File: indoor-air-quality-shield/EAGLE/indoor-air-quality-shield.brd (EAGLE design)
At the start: 160 x 100 mm, 36 parts, among them J4 POWER_JACKSLT, Q1 MMBT2222A, U6 AP1509-50SG-13

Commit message: upadted pcb layout
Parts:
- removed C10: 100uF, 10V, SparkFun-Capacitors:PANASONIC_D
- removed C8: 10nF, SparkFun-Capacitors:0603-CAP
- removed C9: 47uF, 25V, SparkFun-Capacitors:PANASONIC_D
- removed J4: POWER_JACKSLT, Spark:POWER_JACK_SLOT
- removed JP5: M02PTH3, SparkFun-Connectors:1X02_LONGPADS
- removed LED5: BLUE, SparkFun-LED:LED-0603
- removed R13: 1K, SparkFun-Passives:0603-RES
- removed R14, R15: (no value), pot:RJ9W
- removed R16: (no value), SparkFun-Passives:0603-RES
- removed U6: AP1509-50SG-13, Spark:SO08
- added C1: 47uF, 25V, SparkFun-Capacitors:PANASONIC_D
- added C2: 100uF, 10V, SparkFun-Capacitors:PANASONIC_D
- added C3: 10nF, SparkFun-Capacitors:0603-CAP
- added J3: (no value), Connector:4P-2.0
- added JP2: (no value), SparkFun-Connectors:1X03
- added LED1: BLUE, SparkFun-LED:LED-0603
- added R10: 10K, SparkFun-Passives:0603-RES
- added R7, R8, R9: 1K, SparkFun-Passives:0603-RES
- added U1: AP1509-50SG-13, Spark:SO08
- D1: value LED-RGB-CC-THRUCLEAR -> B230; device SparkFun-LED:LED-RGB-THRU -> adafruit:SMADIODE
- D3: value B230 -> LED-RGB-CC-THRUCLEAR; device adafruit:SMADIODE -> SparkFun-LED:LED-RGB-THRU
- J1: value (none) -> POWER_JACKSLT; device Connector:4P-2.0 -> Spark:POWER_JACK_SLOT
- JP1: value (none) -> M02PTH3; device SparkFun-Connectors:1X03 -> SparkFun-Connectors:1X02_LONGPADS
- R1, R2, R3, R4: value (none) -> 50K; device SparkFun-Passives:0603-RES -> pot:RJ9W
- R11, R12: value (none) -> 10K; device pot:RJ9W -> SparkFun-Passives:0603-RES
- R5, R6: value (none) -> 1K
- U$1: value SPARK_CORE -> MQ_SENSOR_SOCKET; device Spark:SPARK_CORE_STACKABLE -> Spark:MQ_SENSOR_SOCKET
- U$3: value MICS5525 -> MQ_SENSOR_SOCKET; device Spark:MICS5525 -> Spark:MQ_SENSOR_SOCKET
- U$4: value MQ_SENSOR_SOCKET -> MICS5525; device Spark:MQ_SENSOR_SOCKET -> Spark:MICS5525
- U$5: value MQ_SENSOR_SOCKET -> DHT22; device Spark:MQ_SENSOR_SOCKET -> Spark:DHT22
- U$6: value DHT22 -> SPARK_CORE; device Spark:DHT22 -> Spark:SPARK_CORE_STACKABLE
- moved JP1 195.4 mm to (99.1, 66.0), turned to 180 degrees
- moved J1 167.7 mm to (102.9, 62.2)
- moved D1 164.8 mm to (106.4, 79.8), turned to 180 degrees
- moved R5 156.6 mm to (125.7, 81.3), turned to 90 degrees
- moved S2 155.4 mm to (82.5, 67.3), turned to 270 degrees
- moved L1 151.3 mm to (119.4, 75.4)
- moved U$6 149.1 mm to (20.3, 81.3), turned to 180 degrees
- moved S1 141.4 mm to (76.2, 67.3), turned to 90 degrees
- moved D2 137.0 mm to (119.1, 82.8)
- moved U$5 135.8 mm to (72.4, 91.4), turned to 270 degrees
- moved R12 135.5 mm to (17.8, 96.5), turned to 180 degrees
- moved U$2 121.1 mm to (63.5, 95.2)
- moved Q1 120.3 mm to (81.3, 73.7), turned to 270 degrees
- moved D3 119.1 mm to (90.2, 66.0), turned to 90 degrees
- moved R6 116.6 mm to (81.3, 77.5)
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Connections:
- net +3V3: now also R10.2, U$5.VDD, U$6.#24, U$6.24, U$6.@24; no longer R16.2, U$1.#24, U$1.24, U$1.@24, U$6.VDD
- net +5V: now also C2.+, C3.2, J3.3, R11.2, R12.2, U$1.5, U$1.6, U$1.7, U$3.5, U$3.6, U$3.7, U$4.H+, U$4.S+, U$6.#1, U$6.1, U$6.@1, U1.3; no longer C10.+, C8.2, J1.3, R13.2, R4.2, U$1.#1, U$1.1, U$1.@1, U$3.H+, U$3.S+, U$4.5, U$4.6, U$4.7, U$5.5, U$5.6, U$5.7, U6.3
- net 3V3*: now also U$6.#22, U$6.22, U$6.@22; no longer U$1.#22, U$1.22, U$1.@22
- net BLUE: now also R7.2, U$6.#5, U$6.5, U$6.@5; no longer R3.2, U$1.#5, U$1.5, U$1.@5
- net BTN1: now also U$6.#16, U$6.16, U$6.@16; no longer U$1.#16, U$1.16, U$1.@16
- net BTN2: now also U$6.#17, U$6.17, U$6.@17; no longer U$1.#17, U$1.17, U$1.@17
- net BUZZER: now also U$6.#8, U$6.8, U$6.@8
- net DHT22: now also R10.1, U$5.DATA, U$6.#15, U$6.15, U$6.@15; no longer R16.1, U$1.#15, U$1.15, U$1.@15, U$6.DATA
- net GND: now also C1.-, C2.-, C3.1, D3.2, J1.GND@1, J1.GND@2, J3.4, JP2.1, LED1.C, R1.A, R1.S, R2.A, R2.S, R3.A, R3.S, R4.A, R4.S, U$4.H-, U$5.GND, U$6.#2, U$6.#21, U$6.2, U$6.21, U$6.@2, U$6.@21, U1.4, U1.5, U1.6, U1.7, U1.8; no longer C10.-, C8.1, C9.-, D1.2, J1.4, J4.GND@1, J4.GND@2, JP5.1, LED5.C, R11.A, R11.S, R12.A, R12.S, R14.A, R14.S, R15.A, R15.S, U$1.#2, U$1.#21, U$1.2, U$1.21, U$1.@2, U$1.@21, U$3.H-, U$6.GND, U6.4, U6.5, U6.6, U6.7, U6.8
- net GREEN: now also R8.2, U$6.#6, U$6.6, U$6.@6; no longer R2.2, U$1.#6, U$1.6, U$1.@6
- net MICS: now also R3.E, U$4.S-, U$6.#11, U$6.11, U$6.@11; no longer R12.E, U$1.#11, U$1.11, U$1.@11, U$3.S-
- net MQ1: now also R2.E, U$1.1, U$1.3, U$6.#10, U$6.10, U$6.@10; no longer R14.E, U$1.#10, U$1.10, U$1.@10, U$4.1, U$4.3
- net MQ2: now also R4.E, U$3.1, U$3.3, U$6.#9, U$6.9, U$6.@9; no longer R15.E, U$1.#9, U$1.9, U$1.@9, U$5.1, U$5.3
- net N$1: now also D3.4, R7.1; no longer D1.4, R3.1
- net N$14: now also C1.+, D1.C, U1.1; no longer C9.+, D3.C, U6.1
- net N$16: now also LED1.A, R5.1; no longer LED5.A, R13.1
- net N$2: now also D3.3, R8.1; no longer D1.3, R2.1
- net N$3: now also D3.1, R9.1; no longer D1.1, R1.1
- net N$32: now also D1.A, J1.PWR, JP1.2; no longer D3.A, J4.PWR, JP5.2
- net N$34: now also U1.2; no longer U6.2
- net RED: now also R9.2, U$6.#7, U$6.7, U$6.@7; no longer R1.2, U$1.#7, U$1.7, U$1.@7
- net SCL: now also J3.1, R11.1, U$6.#14, U$6.14, U$6.@14; no longer J1.1, R4.1, U$1.#14, U$1.14, U$1.@14
- net SDA: now also J3.2, R12.1, U$6.#13, U$6.13, U$6.@13; no longer J1.2, R5.1, U$1.#13, U$1.13, U$1.@13
- net TGS: now also R1.E, U$6.#12, U$6.12, U$6.@12; no longer R11.E, U$1.#12, U$1.12, U$1.@12
- net UART_RX: now also JP2.3, U$6.#4, U$6.4, U$6.@4; no longer JP1.3, U$1.#4, U$1.4, U$1.@4
- net UART_TX: now also JP2.2, U$6.#3, U$6.3, U$6.@3; no longer JP1.2, U$1.#3, U$1.3, U$1.@3
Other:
- board size 160 x 100 mm -> 130.8 x 38.1 mm

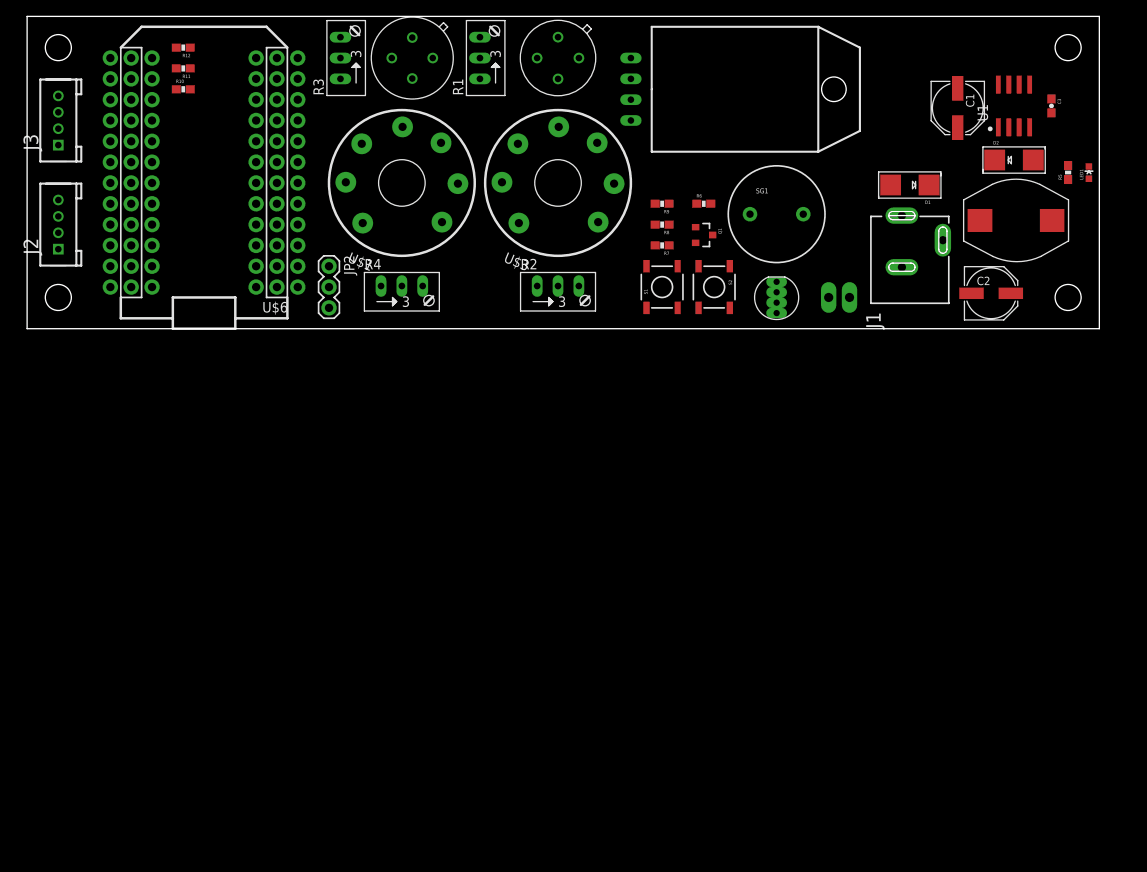
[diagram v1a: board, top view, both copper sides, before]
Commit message: layed out indoor air quality pcb
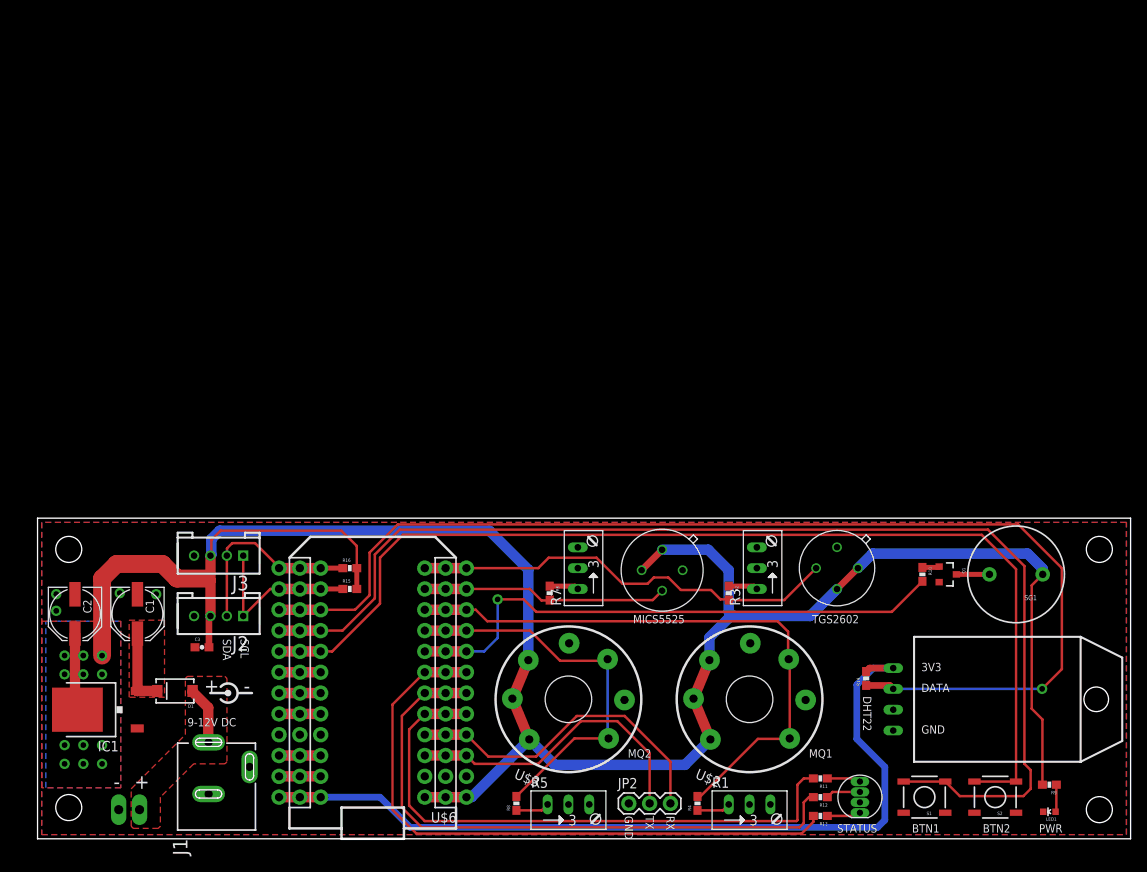
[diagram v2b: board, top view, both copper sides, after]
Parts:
- removed D3: LED-RGB-CC-THRUCLEAR, SparkFun-LED:LED-RGB-THRU
- removed L1: SDR1005-470KL, Spark:INDUCTOR-SDR1005-470KL
- removed U1: AP1509-50SG-13, Spark:SO08
- added IC1: MC33269D-5.0, linear:DPACK
- added R13: 1K, SparkFun-Passives:0603-RES
- added R14, R15, R16: 10K, SparkFun-Passives:0603-RES
- C2: value 100uF, 10V -> 47uF, 25V
- D1: value B230 -> MBRA140; device adafruit:SMADIODE -> SparkFun-DiscreteSemi:SMA-DIODE
- D2: value B230 -> LED-RGB-CC-THRUCLEAR; device adafruit:SMADIODE -> SparkFun-LED:LED-RGB-THRU
- R10, R11, R12: value 10K -> 1K
- R2, R4: value 50K -> (none); device pot:RJ9W -> SparkFun-Resistors:0603-RES
- R5, R7: value 1K -> 50K; device SparkFun-Passives:0603-RES -> pot:RJ9W
- R6, R8: value 1K -> (none); device SparkFun-Passives:0603-RES -> SparkFun-Resistors:0603-RES
- U$1: value MQ_SENSOR_SOCKET -> TGS2602; device Spark:MQ_SENSOR_SOCKET -> Spark:TGS2602
- U$2: value TGS2602 -> MQ_SENSOR_SOCKET; device Spark:TGS2602 -> Spark:MQ_SENSOR_SOCKET
- moved C3 122.9 mm to (20.1, 23.4), turned to 0 degrees
- moved R12 120.0 mm to (95.5, 5.08)
- moved C2 118.4 mm to (4.57, 27.4), turned to 270 degrees
- moved C1 117.6 mm to (12.2, 27.4)
- moved R11 116.4 mm to (95.5, 7.37)
- moved JP1 108.9 mm to (9.91, 3.56), turned to 0 degrees
- moved D1 108.9 mm to (16.8, 18.0)
- moved R10 107.9 mm to (108.0, 32.3), turned to 270 degrees
- moved J1 106.2 mm to (18.3, -2.03)
- moved R5 98.8 mm to (64.8, 3.56), turned to 0 degrees
- moved R1 97.2 mm to (86.9, 3.56), turned to 0 degrees
- moved R9 85.2 mm to (123.4, 6.60)
- moved U$2 81.6 mm to (86.9, 17.0), turned to 337.5 degrees
- moved U$5 81.0 mm to (104.4, 17.0)
- moved R3 80.3 mm to (88.4, 33.0)
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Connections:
- net 3V3* renamed N$9
- removed net N$14: C1.+, D1.C, U1.1
- removed net N$34: D2.C, L1.P$1, U1.2
- new net N$10: R5.E, R8.1
- new net N$11: U$6.#20, U$6.20, U$6.@20
- new net N$12: U$6.#19, U$6.19, U$6.@19
- new net N$13: U$6.#18, U$6.18, U$6.@18
- new net N$4: R2.1, R3.E
- new net N$5: U$6.#23, U$6.23, U$6.@23
- new net N$6: C1.+, D1.C, IC1.3
- new net N$7: R6.1, R7.E
- new net N$8: R1.E, R4.1
- net +3V3: now also R14.2; no longer R10.2
- net +5V: now also IC1.2, R15.2, R16.2, R9.2, U$1.HEATER+, U$1.SENSOR+, U$2.5, U$2.6, U$2.7; no longer L1.P$2, R11.2, R12.2, R5.2, U$1.5, U$1.6, U$1.7, U$2.HEATER+, U$2.SENSOR+, U1.3
- net BLUE: now also R11.2; no longer R7.2
- net BUZZER: now also R10.2; no longer R6.2
- net DHT22: now also R14.1; no longer R10.1
- net GND: now also D2.2, IC1.1, R5.A, R5.S, R7.A, R7.S, U$1.HEATER-, U$2.2, U$3.2; no longer D2.A, D3.2, R2.A, R2.S, R4.A, R4.S, U$2.HEATER-, U1.4, U1.5, U1.6, U1.7, U1.8
- net GREEN: now also R12.2; no longer R8.2
- net MICS: now also R6.2; no longer R3.E
- net MQ1: now also R4.2, U$2.1, U$2.3; no longer R2.E, U$1.1, U$1.3
- net MQ2: now also R8.2; no longer R4.E
- net N$1: now also D2.4, R11.1; no longer D3.4, R7.1
- net N$15: now also R10.1; no longer R6.1
- net N$16: now also R9.1; no longer R5.1
- net N$2: now also D2.3, R12.1; no longer D3.3, R8.1
- net N$3: now also D2.1, R13.1; no longer D3.1, R9.1
- net RED: now also R13.2; no longer R9.2
- net SCL: now also R15.1; no longer R11.1
- net SDA: now also R16.1; no longer R12.1
- net TGS: now also R2.2, U$1.SENSOR-; no longer R1.E, U$2.SENSOR-
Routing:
- net +5V: track 0.00 -> 280.9 mm, vias 0 -> 12
- net BTN1: track 0.00 -> 145.1 mm
- net DHT22: track 0.00 -> 142.4 mm, vias 0 -> 1
- net BTN2: track 0.00 -> 131.8 mm
- net +3V3: track 0.00 -> 102.5 mm
- net RED: track 0.00 -> 77.3 mm
- net GREEN: track 0.00 -> 74.4 mm
- net MQ1: track 0.00 -> 72.7 mm
- net BLUE: track 0.00 -> 71.8 mm
- net BUZZER: track 0.00 -> 68.3 mm, vias 0 -> 1
- net TGS: track 0.00 -> 52.7 mm
- net MQ2: track 0.00 -> 47.9 mm
- net UART_RX: track 0.00 -> 40.5 mm
- net UART_TX: track 0.00 -> 37.7 mm
- net MICS: track 0.00 -> 30.0 mm
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- added copper zone on layer 1, net +5V
- added copper zone on layer 16, net +5V
- added copper zone on layer 1, net GND
- added copper zone on layer 16, net GND
- added copper zone on layer 1, net N$32
- added copper zone on layer 1, net N$6
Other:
- board size 130.8 x 38.1 mm -> 133.3 x 39.1 mm
- board text added: "+"
- board text added: "-"
- board text added: "3V3"
- board text added: "9-12V DC"
- board text added: "BTN1"
- board text added: "BTN2"
- board text added: "DATA"
- board text added: "DHT22"
- board text added: "GND"
- board text added: "INDOOR AIR QUALITY MONITOR"
- board text added: "MICS5525"
- board text added: "MQ1"
- board text added: "MQ2"
- board text added: "PWR"
- board text added: "RX"
- board text added: "SCL"
- board text added: "SDA"
- board text added: "STATUS"
- board text added: "TGS2602"
- board text added: "TX"
- board text added: "spark.io"
- board text added: "v0.1.0"

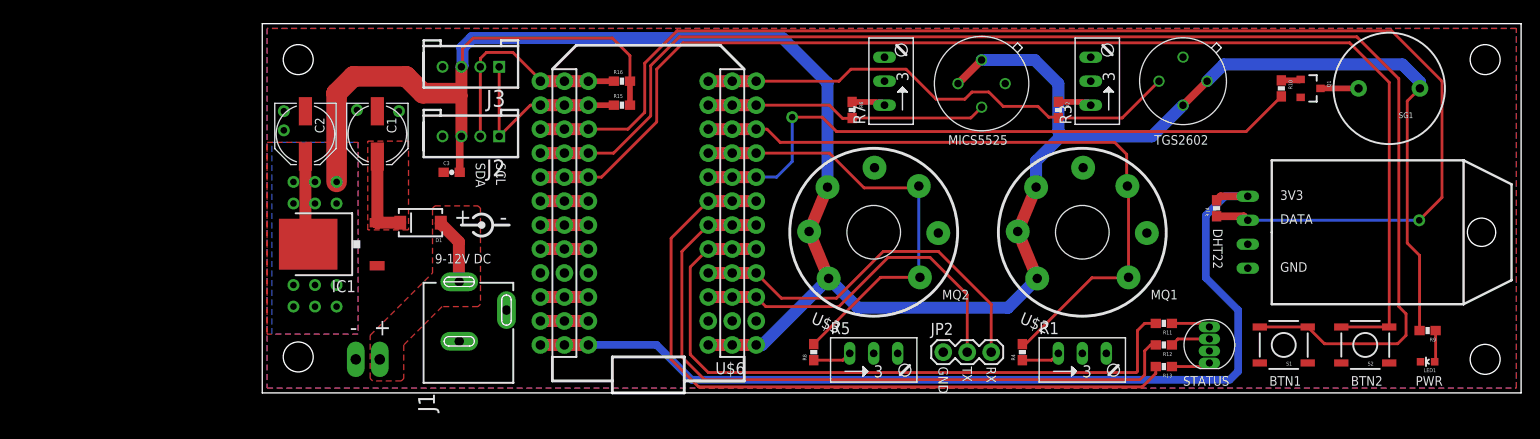
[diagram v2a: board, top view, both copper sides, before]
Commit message: updated aq shield
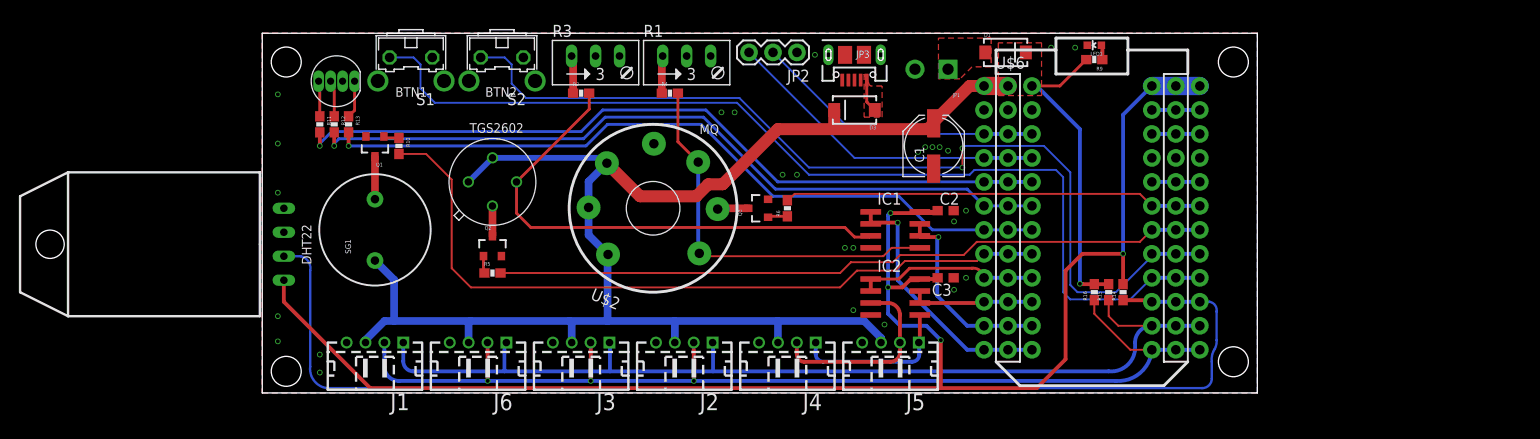
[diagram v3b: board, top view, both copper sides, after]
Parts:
- removed R7: 50K, pot:RJ9W
- removed R8: (no value), SparkFun-Resistors:0603-RES
- removed U$3: MQ_SENSOR_SOCKET, Spark:MQ_SENSOR_SOCKET
- removed U$4: MICS5525, Spark:MICS5525
- added D3: MBRA140, SparkFun-DiscreteSemi:SMA-DIODE
- added IC2: LM358D, linear:SO08
- added J4, J5, J6: (no value), Connector:4P-2.0-90D-W/O-BUCKLE
- added JP3: USBUSB-MICROB-SLOT-HOLE, Spark:USB-MICROB-SLOT-HOLE
- added Q2, Q3: MMBT2222A, SparkFun-DiscreteSemi:SOT23-3
- C2: value 47uF, 25V -> (none); device SparkFun-Capacitors:PANASONIC_D -> rcl:C0603
- C3: value 10nF -> (none); device SparkFun-Capacitors:0603-CAP -> rcl:C0603
- IC1: value MC33269D-5.0 -> LM358D; device linear:DPACK -> linear:SO08
- J1: value POWER_JACKSLT -> (none); device Spark:POWER_JACK_SLOT -> Connector:4P-2.0-90D-W/O-BUCKLE
- J2, J3: device Connector:4P-2.0 -> Connector:4P-2.0-90D-W/O-BUCKLE
- JP1: value M02PTH3 -> M023.5MM-NO_SILK; device SparkFun-Connectors:1X02_LONGPADS -> SparkFun-Connectors:SCREWTERMINAL-3.5MM-2-NS
- R5: value 50K -> 1K; device pot:RJ9W -> SparkFun-Passives:0603-RES
- R6: value (none) -> 1K; device SparkFun-Resistors:0603-RES -> SparkFun-Passives:0603-RES
- S1, S2: device SparkFun-Electromechanical:TACTILE_SWITCH_SMD -> switch-omron:B3F-31XX
- moved SG1 108.5 mm to (11.9, 17.3), turned to 90 degrees
- moved U$5 102.1 mm to (2.29, 15.7), turned to 90 degrees
- moved Q1 99.2 mm to (11.9, 26.2), turned to 180 degrees
- moved S1 97.0 mm to (15.7, 34.3)
- moved D2 96.6 mm to (7.87, 33.0), turned to 0 degrees
- moved S2 96.0 mm to (25.4, 34.3)
- moved R10 93.7 mm to (14.5, 26.2)
- moved R11 91.9 mm to (6.10, 28.4), turned to 270 degrees
- moved R12 90.9 mm to (7.62, 28.4), turned to 270 degrees
- moved R13 90.1 mm to (9.14, 28.4), turned to 270 degrees
- moved U$1 73.9 mm to (24.4, 22.4), turned to 180 degrees
- moved JP1 69.9 mm to (72.6, 34.3), turned to 180 degrees
- moved C2 68.3 mm to (72.4, 19.3), turned to 0 degrees
- moved D1 64.5 mm to (78.7, 36.1), turned to 0 degrees
- moved IC1 59.7 mm to (67.1, 17.3), turned to 270 degrees
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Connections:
- net N$11 renamed D7
- removed net MICS: R6.2, U$4.S-, U$6.#11, U$6.11, U$6.@11
- removed net MQ1: R4.2, U$2.1, U$2.3, U$6.#10, U$6.10, U$6.@10
- removed net MQ2: R8.2, U$3.1, U$3.3, U$6.#9, U$6.9, U$6.@9
- removed net N$12: U$6.#19, U$6.19, U$6.@19
- removed net N$13: U$6.#18, U$6.18, U$6.@18
- removed net N$32: D1.A, J1.PWR, JP1.2
- new net A2: IC2.6, IC2.7, U$6.#10, U$6.10, U$6.@10
- new net A3: IC2.1, IC2.2, U$6.#9, U$6.9, U$6.@9
- new net D5: R5.2, U$6.#18, U$6.18, U$6.@18
- new net D6: R6.2, U$6.#19, U$6.19, U$6.@19
- new net FA1: IC2.5, J4.1, J5.1
- new net FA2: IC2.3, J4.2, J5.2
- new net MQ: IC1.6, IC1.7, U$6.#11, U$6.11, U$6.@11
- new net N$11: IC1.3, R2.2, U$1.SENSOR-
- new net N$14: Q3.1, R6.1
- new net N$18: Q2.3, U$1.HEATER-
- new net N$19: Q2.1, R5.1
- new net N$23: IC1.5, R4.2, U$2.1, U$2.3
- net +3V3: now also C2.1, C3.2, IC1.8, IC2.8
- net +5V: now also C1.+, D1.C, D3.C, J1.3, J4.3, J5.3, J6.3; no longer C2.+, C3.2, IC1.2, U$3.5, U$3.6, U$3.7, U$4.H+, U$4.S+
- net BTN1: now also S1.2; no longer S1.3, S1.4
- net BTN2: now also S2.2; no longer S2.3, S2.4
- net GND: now also C2.2, IC1.4, IC2.4, J1.4, J4.4, J5.4, J6.4, JP1.2, JP3.GND, JP3.MT1, JP3.MT2, Q2.2, Q3.2; no longer C2.-, IC1.1, J1.GND@1, J1.GND@2, JP1.1, R5.A, R5.S, R7.A, R7.S, S1.2, S2.2, U$1.HEATER-, U$2.2, U$3.2, U$4.H-
- net N$10: now also D3.A, JP3.VBUS; no longer R5.E, R8.1
- net N$6: now also D1.A, JP1.1; no longer C1.+, D1.C, IC1.3
- net N$7: now also Q3.3, U$2.2; no longer R6.1, R7.E
- net SCL: now also J1.1, J6.1
- net SDA: now also J1.2, J6.2
- net TGS: now also IC1.1, IC1.2; no longer R2.2, U$1.SENSOR-
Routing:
- net +5V: track 280.9 -> 192.2 mm, vias 12 -> 1
- net SDA: track 24.0 -> 112.1 mm, vias 0 -> 3
- net SCL: track 20.9 -> 105.2 mm
- net D5: track 0.00 -> 76.0 mm
- net MQ1: track 72.7 -> 0.00 mm
- net +3V3: track 102.5 -> 169.0 mm, vias 0 -> 4
- net N$11: track 0.00 -> 54.5 mm
- net MQ2: track 47.9 -> 0.00 mm
- net D6: track 0.00 -> 44.5 mm
- net N$23: track 0.00 -> 41.8 mm
- net BTN1: track 145.1 -> 106.4 mm
- net BTN2: track 131.8 -> 99.6 mm, vias 0 -> 2
- net MICS: track 30.0 -> 0.00 mm
- net TGS: track 52.7 -> 27.5 mm, vias 0 -> 1
- net MQ: track 0.00 -> 20.9 mm, vias 0 -> 1
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- added copper zone on layer 1, net N$10
- removed copper zone on layer 16, net +5V
- removed copper zone on layer 1, net N$32
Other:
- board size 133.3 x 39.1 mm -> 105.4 x 38.1 mm
- board text added: "MQ"
- board text removed: "+"
- board text removed: "-"
- board text removed: "3V3"
- board text removed: "9-12V DC"
- board text removed: "DATA"
- board text removed: "GND"
- board text removed: "INDOOR AIR QUALITY MONITOR"
- board text removed: "MICS5525"
- board text removed: "MQ1"
- board text removed: "MQ2"
- board text removed: "PWR"
- board text removed: "RX"
- board text removed: "SCL"
- board text removed: "SDA"
- board text removed: "STATUS"
- board text removed: "TX"
- board text removed: "v0.1.0"

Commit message: added labels and did cleanup
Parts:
- added U$3: (no value), Spark:SPARK_LOGO2
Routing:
- net GND: track 0.00 -> 8.03 mm, vias 27 -> 26
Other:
- outline, holes or cut-outs redrawn
- board text added: "+5V"
- board text added: "3V3"
- board text added: "A2"
- board text added: "A3"
- board text added: "AIR QUALITY SHIELD"
- board text added: "B"
- board text added: "BUZZER"
- board text added: "DO"
- board text added: "G"
- board text added: "GND"
- board text added: "PWR"
- board text added: "R"
- board text added: "RX"
- board text added: "SCL"
- board text added: "SDA"
- board text added: "TGS"
- board text added: "TX"
